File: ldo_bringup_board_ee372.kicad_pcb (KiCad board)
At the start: 4 copper layers, 100 x 100 mm, 152 parts, among them J1 VIN, J10 MD_SW_EN, J11 MD_MCU_PU_EN, J12 BUF_EN, J13 VSIG, J14 VSIG_BUF, J15 NR, J16 NOISE_X100, J17 NOISE_X1000, J18 VIN_PROBE, J19 VREF_PROBE, J2 GND, J20 VOUT_PROBE, J21 VG0_PROBE, J22 VG1_PROBE, J23 VG2_PROBE, J24 VG3_PROBE, J25 VG4_PROBE, J3 IBIAS, J4 VOUT, J5 VIN_SMA, J6 VOUT_SMA, J7 GND, J8 5V, J9 MD_MCU_EN, Q1 FDV305N, Q2 FDV305N, Q3 FDV305N, Q4 FDV305N, Q5 FDV305N, Q6 FDV305N, SW1 MD_SW, U1 LDO_DualMode_BGR_EE372, U2 Teensy4.1, U3 INA190A5IDDFR, U4 INA190A5IDDFR, U5 OPA4388IDR, U6 BUF602ID, U7 ADT7310TRZ

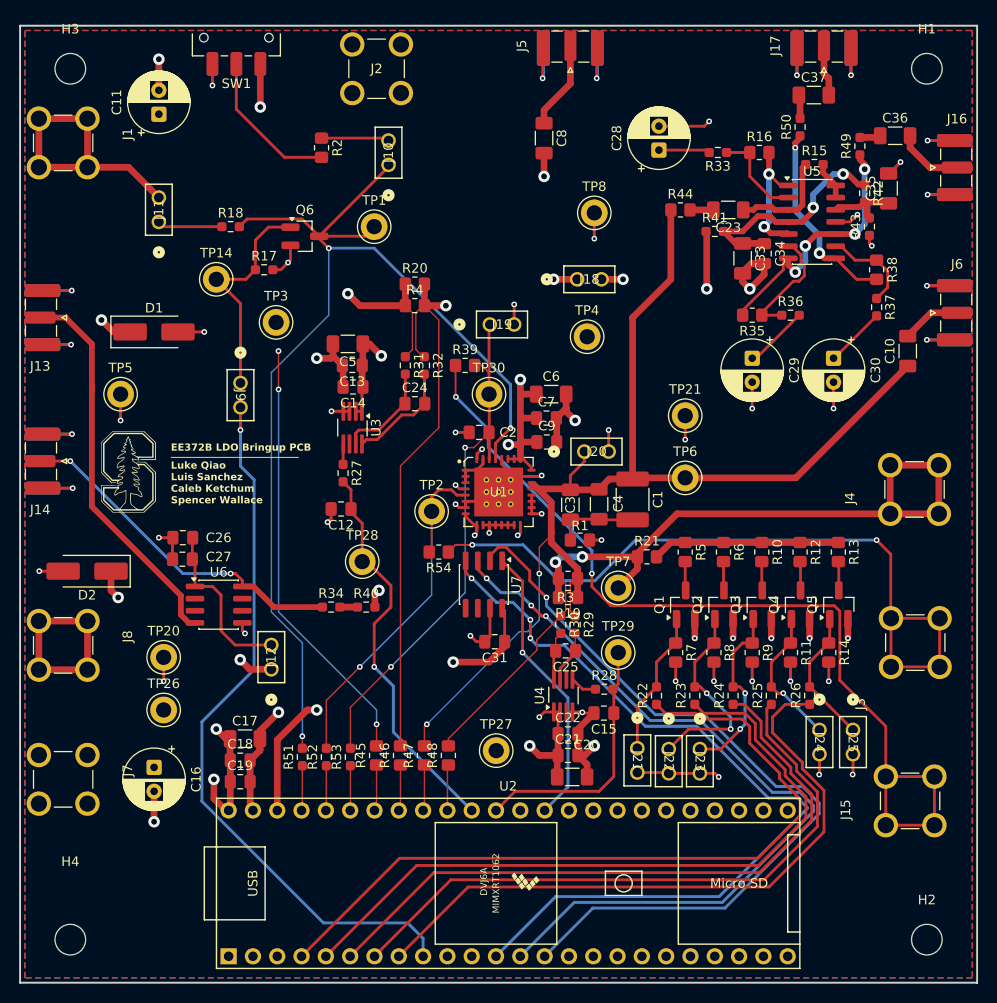
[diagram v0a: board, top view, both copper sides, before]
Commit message: Add 143 GND stitching vias between the F.Cu and B.Cu pours
Placed by script on a 5 mm grid, only where both outer GND pours already
have copper, 0.45 mm inside the pour edge and 0.8 mm clear of every pad
and existing via. 0.6 mm pad, 0.3 mm drill. Zones refilled.

Parts, tracks, existing vias and zone outlines are unchanged.
Vias 128 to 271. DRC 0 errors, 0 unconnected, schematic parity 0.

Co-Authored-By: Claude Opus 5.5 (1M context) <noreply@anthropic.com>
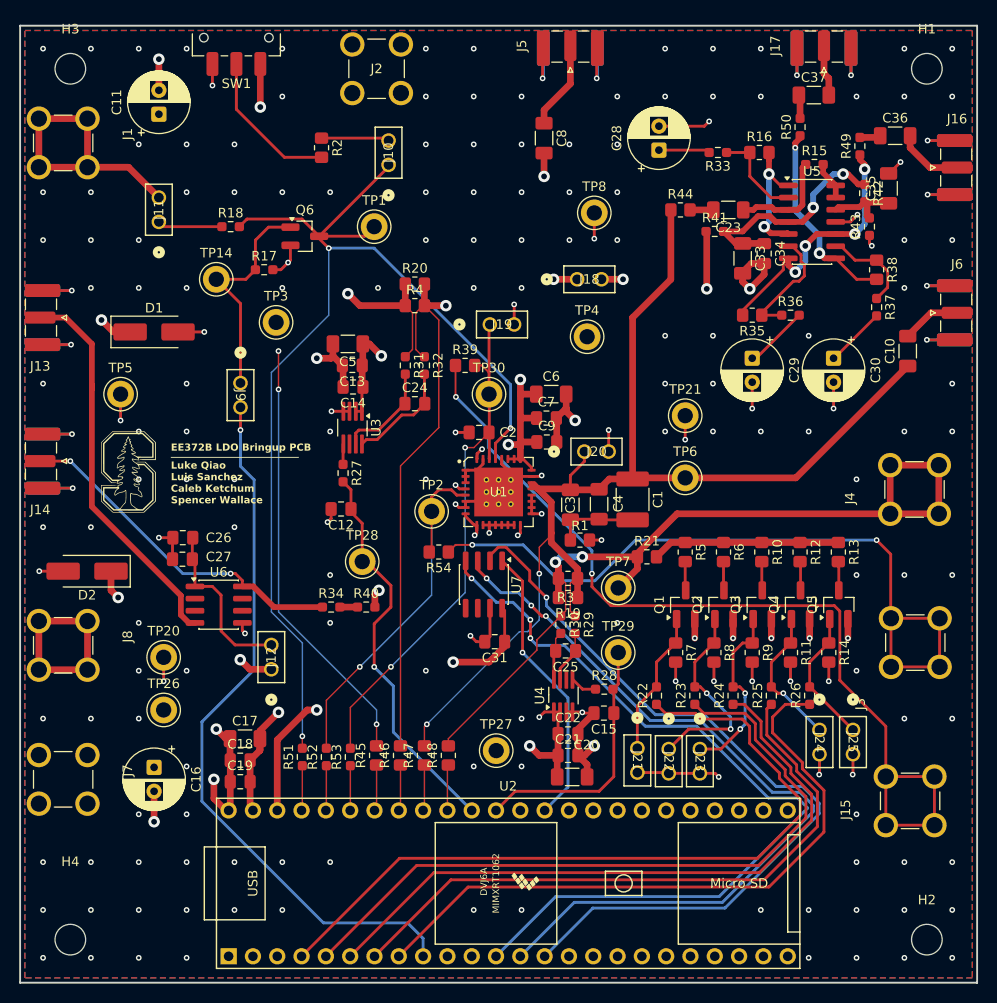
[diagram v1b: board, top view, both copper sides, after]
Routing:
- net GND: vias 61 -> 204

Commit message: Add 189 more GND vias: return vias at layer changes, tighter stitching
Placed by script, only where both outer GND pours already have copper.
0.6 mm pad, 0.3 mm drill. Zones refilled.

- 32 vias within 2 mm of signal and power vias that had no ground via
  nearby. 28 of 67 such vias still have none, no legal spot exists.
- 157 vias on a 1.25 mm grid wherever the nearest ground via or pin was
  over 3.2 mm away.

Pour area over 5 mm from a ground via: F.Cu 10.9% to 1.2%, B.Cu 17.1%
to 4.2%. Parts, tracks, existing vias and zone outlines are unchanged.
Vias 271 to 460. DRC 0 errors, 0 unconnected, schematic parity 0.

Co-Authored-By: Claude Opus 5.5 (1M context) <noreply@anthropic.com>
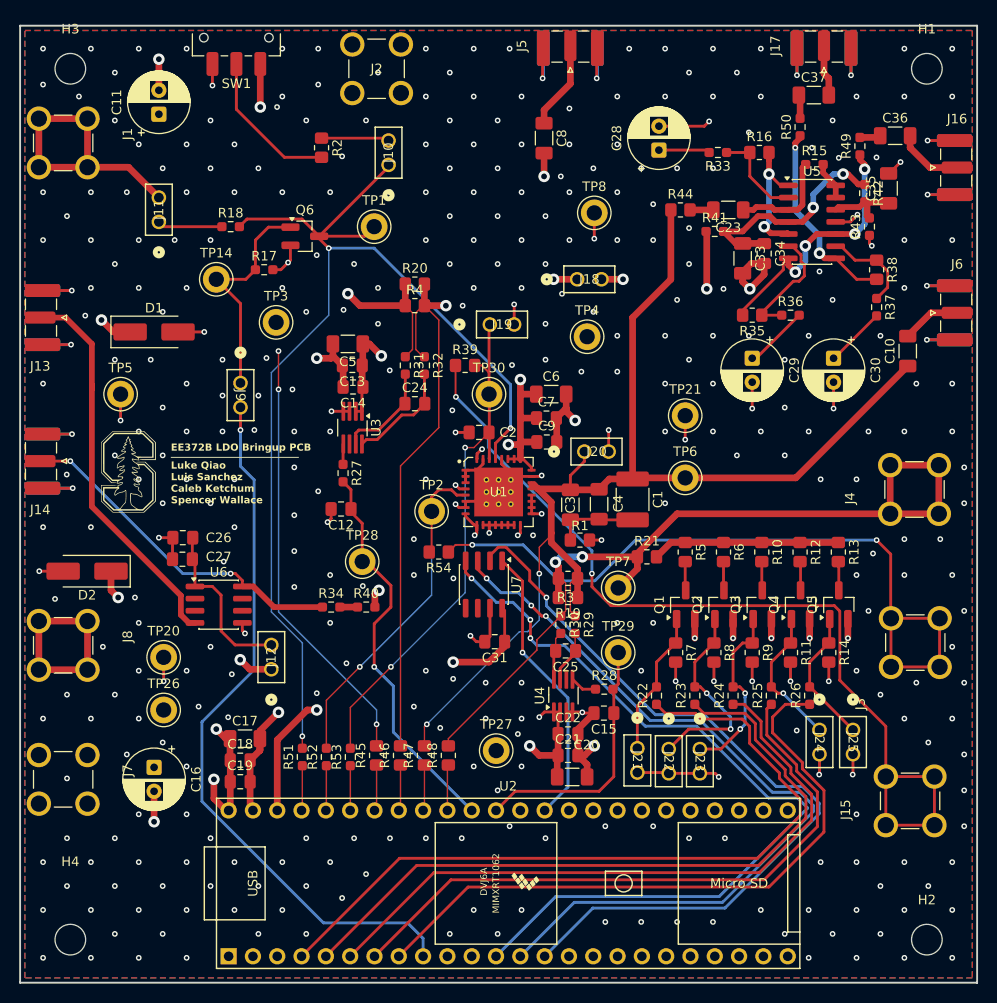
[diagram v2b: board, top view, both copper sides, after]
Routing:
- net GND: vias 204 -> 393
